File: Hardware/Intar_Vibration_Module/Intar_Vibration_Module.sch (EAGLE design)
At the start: 8 parts, among them J2 GROVE-4P-2.0-3470130P1, M1 MOTORVIBE_COIN_SMD

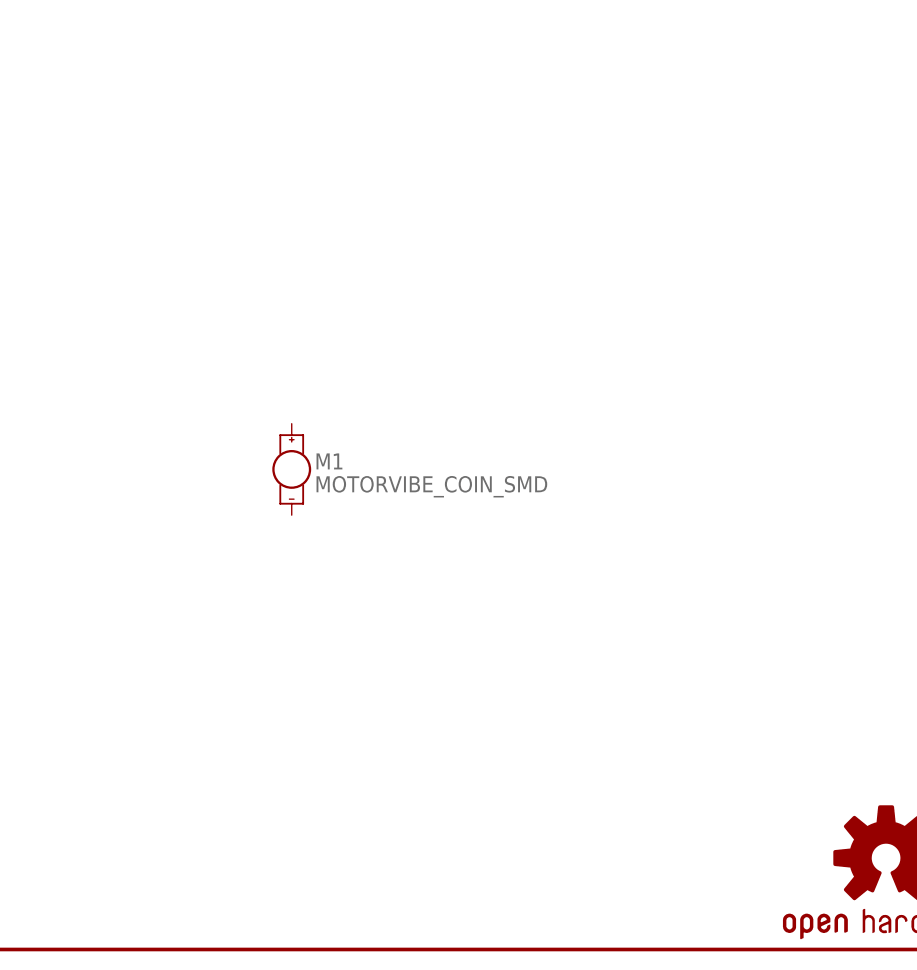
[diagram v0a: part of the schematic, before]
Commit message: Created schematics for first round of modules.
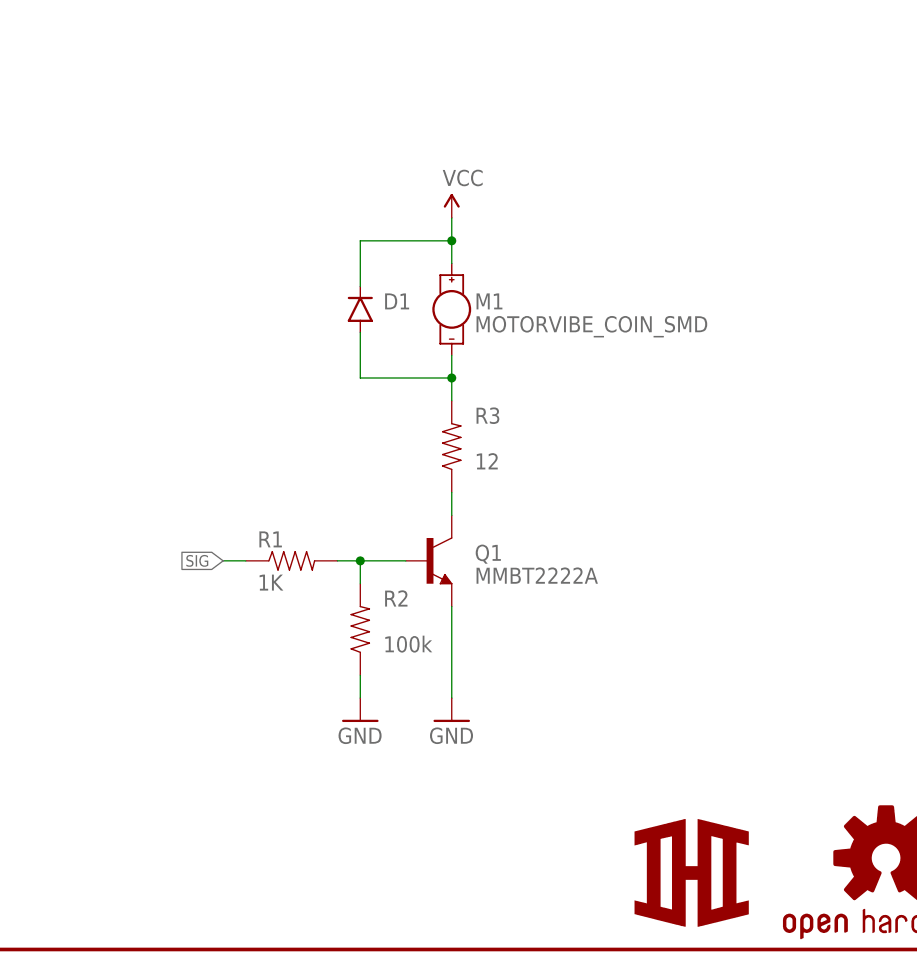
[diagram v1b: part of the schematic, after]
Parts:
- added D1: (no value), SparkFun-DiscreteSemi:DIODESMB
- added Q1: MMBT2222A, SparkFun-DiscreteSemi:TRANSISTOR_NPNMMBT2222A
- added R1: 1K, SparkFun-Resistors:1KOHM-1/10W-1%(0603)
- added R2: 100k, SparkFun-Resistors:100KOHM-1/10W-1%(0603)
- added R3: 12, SparkFun-Resistors:RESISTOR0603
- added U$1: LOGOSM, Intar_Eagle_Library:LOGOSM
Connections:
- new net N$2: Q1.B, R1.2, R2.2
- new net N$5: Q1.C, R3.1
- new net N$6: D1.A, M1.-, R3.2
- net GND: now also Q1.E, R2.1
- net SIG: now also R1.1
- net VCC: now also D1.C, M1.+
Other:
- moved on the sheet: M1
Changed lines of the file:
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@@
 <setting verticaltext="up"/>
 </settings>
-<grid distance="0.1" unitdist="inch" unit="inch" style="lines" multiple="1" display="no" altdistance="0.01" altunitdist="inch" altunit="inch"/>
+<grid distance="0.1" unitdist="inch" unit="inch" style="lines" multiple="1" display="yes" altdistance="0.01" altunitdist="inch" altunit="inch"/>
 <layers>
 <layer number="1" name="Top" color="4" fill="1" visible="no" active="no"/>
@@
 <part name="SUPPLY5" library="SparkFun-Aesthetics" deviceset="VCC" device=""/>
 <part name="M1" library="Intar_Eagle_Library" deviceset="MOTOR" device="VIBE_COIN_SMD"/>
+<part name="R1" library="SparkFun-Resistors" deviceset="1KOHM-1/10W-1%(0603)" device="" value="1K"/>
+<part name="R2" library="SparkFun-Resistors" deviceset="100KOHM-1/10W-1%(0603)" device="" value="100k"/>
+<part name="R3" library="SparkFun-Resistors" deviceset="RESISTOR" device="0603" value="12"/>
+<part name="D1" library="SparkFun-DiscreteSemi" deviceset="DIODE" device="SMB"/>
+<part name="Q1" library="SparkFun-DiscreteSemi" deviceset="TRANSISTOR_NPN" device="MMBT2222A" value="MMBT2222A"/>
+<part name="SUPPLY1" library="SparkFun-Aesthetics" deviceset="VCC" device=""/>
+<part name="GND1" library="SparkFun-Aesthetics" deviceset="GND" device=""/>
+<part name="GND2" library="SparkFun-Aesthetics" deviceset="GND" device=""/>
+<part name="U$1" library="Intar_Eagle_Library" deviceset="LOGO" device="SM"/>
 </parts>
 <sheets>
@@
 <instance part="GND5" gate="1" x="81.28" y="149.86"/>
 <instance part="SUPPLY5" gate="G$1" x="88.9" y="147.32"/>
-<instance part="M1" gate="G$1" x="66.04" y="53.34"/>
+<instance part="M1" gate="G$1" x="83.82" y="71.12"/>
+<instance part="R1" gate="G$1" x="66.04" y="43.18"/>
+<instance part="R2" gate="G$1" x="73.66" y="35.56" smashed="yes" rot="R90">
+<attribute name="NAME" x="76.2" y="38.1" size="1.778" layer="95"/>
+<attribute name="VALUE" x="76.2" y="33.02" size="1.778" layer="96"/>
+</instance>
+<instance part="R3" gate="G$1" x="83.82" y="55.88" smashed="yes" rot="R90">
+<attribute name="NAME" x="86.36" y="58.42" size="1.778" layer="95"/>
+<attribute name="VALUE" x="86.36" y="53.34" size="1.778" layer="96"/>
+</instance>
+<instance part="D1" gate="G$1" x="73.66" y="71.12" smashed="yes" rot="R90">
+<attribute name="NAME" x="76.2" y="71.12" size="1.778" layer="95"/>
+<attribute name="VALUE" x="75.9714" y="73.66" size="1.778" layer="96" rot="R90"/>
+</instance>
+<instance part="Q1" gate="G$1" x="81.28" y="43.18"/>
+<instance part="SUPPLY1" gate="G$1" x="83.82" y="81.28"/>
+<instance part="GND1" gate="1" x="73.66" y="25.4"/>
+<instance part="GND2" gate="1" x="83.82" y="25.4"/>
+<instance part="U$1" gate="G$1" x="104.14" y="2.54"/>
 </instances>
 <busses>
@@
 <pinref part="GND5" gate="1" pin="GND"/>
 </segment>
+<segment>
+<pinref part="R2" gate="G$1" pin="1"/>
+<wire x1="73.66" y1="30.48" x2="73.66" y2="27.94" width="0.1524" layer="91"/>
+<pinref part="GND1" gate="1" pin="GND"/>
+</segment>
+<segment>
+<pinref part="Q1" gate="G$1" pin="E"/>
+<wire x1="83.82" y1="38.1" x2="83.82" y2="27.94" width="0.1524" layer="91"/>
+<pinref part="GND2" gate="1" pin="GND"/>
+</segment>
 </net>
 <net name="VCC" class="0">
@@
 <pinref part="SUPPLY5" gate="G$1" pin="VCC"/>
 </segment>
+<segment>
+<pinref part="D1" gate="G$1" pin="C"/>
+<wire x1="73.66" y1="73.66" x2="73.66" y2="78.74" width="0.1524" layer="91"/>
+<wire x1="73.66" y1="78.74" x2="83.82" y2="78.74" width="0.1524" layer="91"/>
+<pinref part="M1" gate="G$1" pin="+"/>
+<wire x1="83.82" y1="76.2" x2="83.82" y2="78.74" width="0.1524" layer="91"/>
+<wire x1="83.82" y1="78.74" x2="83.82" y2="81.28" width="0.1524" layer="91"/>
+<junction x="83.82" y="78.74"/>
+<pinref part="SUPPLY1" gate="G$1" pin="VCC"/>
+</segment>
 </net>
 <net name="SIG" class="0">
@@
 <label x="76.2" y="139.7" size="1.27" layer="95" xref="yes"/>
 </segment>
-</net>
+<segment>
+<pinref part="R1" gate="G$1" pin="1"/>
+<wire x1="58.42" y1="43.18" x2="60.96" y2="43.18" width="0.1524" layer="91"/>
+<label x="58.42" y="43.18" size="1.27" layer="95" rot="R180" xref="yes"/>
+</segment>
+</net>
+<net name="N$2" class="0">
+<segment>
+<pinref part="R1" gate="G$1" pin="2"/>
+<pinref part="Q1" gate="G$1" pin="B"/>
+<wire x1="71.12" y1="43.18" x2="73.66" y2="43.18" width="0.1524" layer="91"/>
+<pinref part="R2" gate="G$1" pin="2"/>
+<wire x1="73.66" y1="43.18" x2="78.74" y2="43.18" width="0.1524" layer="91"/>
+<wire x1="73.66" y1="40.64" x2="73.66" y2="43.18" width="0.1524" layer="91"/>
+<junction x="73.66" y="43.18"/>
+</segment>
+</net>
+<net name="N$5" class="0">
+<segment>
+<pinref part="Q1" gate="G$1" pin="C"/>
+<pinref part="R3" gate="G$1" pin="1"/>
+<wire x1="83.82" y1="48.26" x2="83.82" y2="50.8" width="0.1524" layer="91"/>
+</segment>
+</net>
+<net name="N$6" class="0">
+<segment>
+<pinref part="R3" gate="G$1" pin="2"/>
+<pinref part="M1" gate="G$1" pin="-"/>
+<wire x1="83.82" y1="60.96" x2="83.82" y2="63.5" width="0.1524" layer="91"/>
+<pinref part="D1" gate="G$1" pin="A"/>
+<wire x1="83.82" y1="63.5" x2="83.82" y2="66.04" width="0.1524" layer="91"/>
+<wire x1="73.66" y1="68.58" x2="73.66" y2="63.5" width="0.1524" layer="91"/>
+<wire x1="73.66" y1="63.5" x2="83.82" y2="63.5" width="0.1524" layer="91"/>
+<junction x="83.82" y="63.5"/>
+</segment>
+</net>

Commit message: Arranged components on all modules
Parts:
- D1: value (none) -> 250mA/100V; device SparkFun-DiscreteSemi:DIODESMB -> SparkFun-DiscreteSemi:DIODEBAS16
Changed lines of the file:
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@@
 <setting verticaltext="up"/>
 </settings>
-<grid distance="0.1" unitdist="inch" unit="inch" style="lines" multiple="1" display="yes" altdistance="0.01" altunitdist="inch" altunit="inch"/>
+<grid distance="0.1" unitdist="inch" unit="inch" style="lines" multiple="1" display="no" altdistance="0.01" altunitdist="inch" altunit="inch"/>
 <layers>
 <layer number="1" name="Top" color="4" fill="1" visible="no" active="no"/>
@@
 <part name="R2" library="SparkFun-Resistors" deviceset="100KOHM-1/10W-1%(0603)" device="" value="100k"/>
 <part name="R3" library="SparkFun-Resistors" deviceset="RESISTOR" device="0603" value="12"/>
-<part name="D1" library="SparkFun-DiscreteSemi" deviceset="DIODE" device="SMB"/>
+<part name="D1" library="SparkFun-DiscreteSemi" deviceset="DIODE" device="BAS16" value="250mA/100V"/>
 <part name="Q1" library="SparkFun-DiscreteSemi" deviceset="TRANSISTOR_NPN" device="MMBT2222A" value="MMBT2222A"/>
 <part name="SUPPLY1" library="SparkFun-Aesthetics" deviceset="VCC" device=""/>
@@
 <instance part="D1" gate="G$1" x="73.66" y="71.12" smashed="yes" rot="R90">
 <attribute name="NAME" x="76.2" y="71.12" size="1.778" layer="95"/>
-<attribute name="VALUE" x="75.9714" y="73.66" size="1.778" layer="96" rot="R90"/>
 </instance>
 <instance part="Q1" gate="G$1" x="81.28" y="43.18"/>

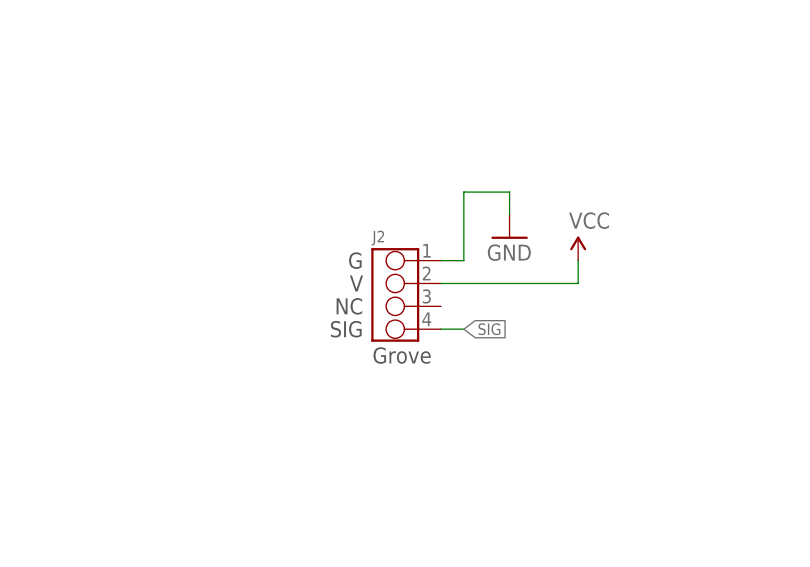
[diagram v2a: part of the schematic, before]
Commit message: Fixed Grove connectors to be right way (pin 4 should be GND)
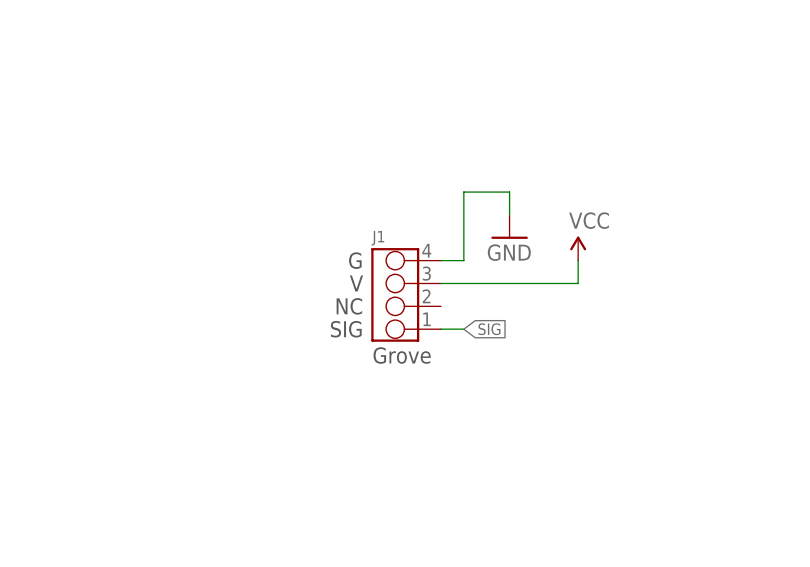
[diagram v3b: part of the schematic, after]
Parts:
- renumbered J2 to J1
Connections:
- net GND: now also J1.4; no longer J1.1
- net SIG: now also J1.1; no longer J1.4
- net VCC: now also J1.3; no longer J1.2
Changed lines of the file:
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@@
 <setting verticaltext="up"/>
 </settings>
-<grid distance="0.1" unitdist="inch" unit="inch" style="lines" multiple="1" display="no" altdistance="0.01" altunitdist="inch" altunit="inch"/>
+<grid distance="0.1" unitdist="inch" unit="inch" style="lines" multiple="1" display="yes" altdistance="0.01" altunitdist="inch" altunit="inch"/>
 <layers>
 <layer number="1" name="Top" color="4" fill="1" visible="no" active="no"/>
@@
 <part name="STANDOFF2" library="SparkFun-Electromechanical" deviceset="STAND-OFF" device=""/>
 <part name="LOGO1" library="SparkFun-Aesthetics" deviceset="OSHW-LOGO" device="S"/>
-<part name="J2" library="Connector" deviceset="GROVE-4P-2.0" device="-3470130P1"/>
 <part name="GND5" library="SparkFun-Aesthetics" deviceset="GND" device=""/>
 <part name="SUPPLY5" library="SparkFun-Aesthetics" deviceset="VCC" device=""/>
@@
 <part name="GND2" library="SparkFun-Aesthetics" deviceset="GND" device=""/>
 <part name="U$1" library="Intar_Eagle_Library" deviceset="LOGO" device="SM"/>
+<part name="J1" library="Connector" deviceset="GROVE-4P-2.0" device="-3470130P1"/>
 </parts>
 <sheets>
@@
 <instance part="STANDOFF2" gate="G$1" x="241.3" y="27.94"/>
 <instance part="LOGO1" gate="G$1" x="132.08" y="10.16"/>
-<instance part="J2" gate="J" x="68.58" y="143.51" smashed="yes">
-<attribute name="NAME" x="66.04" y="149.352" size="1.27" layer="95" ratio="10"/>
-</instance>
 <instance part="GND5" gate="1" x="81.28" y="149.86"/>
 <instance part="SUPPLY5" gate="G$1" x="88.9" y="147.32"/>
@@
 <instance part="GND2" gate="1" x="83.82" y="25.4"/>
 <instance part="U$1" gate="G$1" x="104.14" y="2.54"/>
+<instance part="J1" gate="J" x="68.58" y="143.51" smashed="yes" rot="MR180">
+<attribute name="NAME" x="66.04" y="149.352" size="1.27" layer="95" ratio="10"/>
+</instance>
 </instances>
 <busses>
@@
 <net name="GND" class="0">
 <segment>
-<pinref part="J2" gate="J" pin="1"/>
 <wire x1="73.66" y1="147.32" x2="76.2" y2="147.32" width="0.1524" layer="91"/>
 <wire x1="76.2" y1="147.32" x2="76.2" y2="154.94" width="0.1524" layer="91"/>
@@
 <wire x1="81.28" y1="154.94" x2="81.28" y2="152.4" width="0.1524" layer="91"/>
 <pinref part="GND5" gate="1" pin="GND"/>
+<pinref part="J1" gate="J" pin="4"/>
 </segment>
 <segment>
@@
 <net name="VCC" class="0">
 <segment>
-<pinref part="J2" gate="J" pin="2"/>
 <wire x1="73.66" y1="144.78" x2="88.9" y2="144.78" width="0.1524" layer="91"/>
 <wire x1="88.9" y1="144.78" x2="88.9" y2="147.32" width="0.1524" layer="91"/>
 <pinref part="SUPPLY5" gate="G$1" pin="VCC"/>
+<pinref part="J1" gate="J" pin="3"/>
 </segment>
 <segment>
@@
 <net name="SIG" class="0">
 <segment>
-<pinref part="J2" gate="J" pin="4"/>
 <wire x1="73.66" y1="139.7" x2="76.2" y2="139.7" width="0.1524" layer="91"/>
 <label x="76.2" y="139.7" size="1.27" layer="95" xref="yes"/>
-</segment>
-<segment>
+<pinref part="J1" gate="J" pin="1"/>
+</segment>
+<segment>
